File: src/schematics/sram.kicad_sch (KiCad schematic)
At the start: 4 parts, among them U9 IS61WV25616BLL-*BLI

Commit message: Add remaining component footprints (#79)
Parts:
- C90, C91, C92: footprint (none) -> Capacitor_SMD:C_0402_1005Metric
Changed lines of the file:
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@@
+		(polyline
+			(pts
+				(xy 165.1 74.93) (xy 165.1 115.57) (xy 167.64 115.57) (xy 167.64 74.93)
+			)
+			(stroke
+				(width 0)
+				(type dash)
+			)
+			(fill
+				(type color)
+				(color 255 0 0 0.1)
+			)
+		)
+	)
+	(rule_area
 		(polyline
 			(pts
 				(xy 135.89 64.77) (xy 135.89 124.46) (xy 138.43 124.46) (xy 138.43 64.77)
-			)
-			(stroke
-				(width 0)
-				(type dash)
-			)
-			(fill
-				(type color)
-				(color 255 0 0 0.1)
-			)
-		)
-	)
-	(rule_area
-		(polyline
-			(pts
-				(xy 165.1 74.93) (xy 165.1 115.57) (xy 167.64 115.57) (xy 167.64 74.93)
 			)
 			(stroke
@@
 			)
 		)
-		(property "Footprint" ""
+		(property "Footprint" "Capacitor_SMD:C_0402_1005Metric"
 			(at 166.37 53.34 0)
 			(effects
@@
 			)
 		)
-		(property "Footprint" ""
+		(property "Footprint" "Capacitor_SMD:C_0402_1005Metric"
 			(at 176.53 53.34 0)
 			(effects
@@
 			)
 		)
-		(property "Footprint" ""
+		(property "Footprint" "Capacitor_SMD:C_0402_1005Metric"
 			(at 186.69 53.34 0)
 			(effects

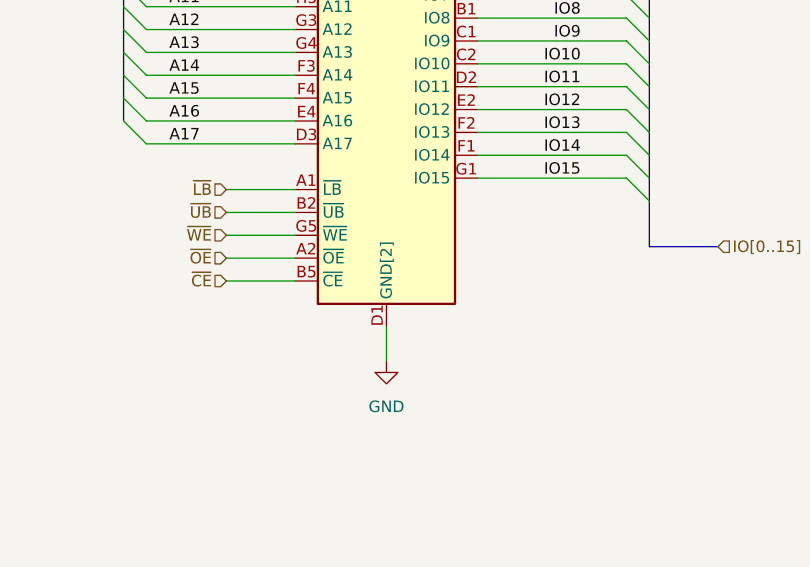
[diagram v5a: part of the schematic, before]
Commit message: Update big inductors for smaller ones
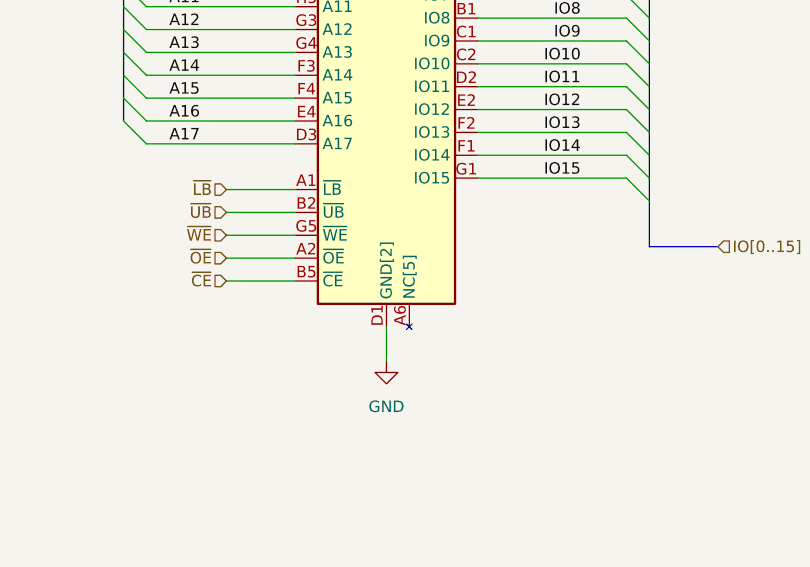
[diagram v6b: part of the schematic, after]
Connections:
- net at U9.A6 (NC[5]), U9.E3 (NC), U9.G2 (NC)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: no longer U9. (NC[5])
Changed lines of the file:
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@@
+		(polyline
+			(pts
+				(xy 135.89 64.77) (xy 135.89 124.46) (xy 138.43 124.46) (xy 138.43 64.77)
+			)
+			(stroke
+				(width 0)
+				(type dash)
+			)
+			(fill
+				(type color)
+				(color 255 0 0 0.1)
+			)
+		)
+	)
+	(rule_area
 		(polyline
 			(pts
 				(xy 165.1 74.93) (xy 165.1 115.57) (xy 167.64 115.57) (xy 167.64 74.93)
-			)
-			(stroke
-				(width 0)
-				(type dash)
-			)
-			(fill
-				(type color)
-				(color 255 0 0 0.1)
-			)
-		)
-	)
-	(rule_area
-		(polyline
-			(pts
-				(xy 135.89 64.77) (xy 135.89 124.46) (xy 138.43 124.46) (xy 138.43 64.77)
 			)
 			(stroke
@@
 		(pin "G5"
 		)
-		(pin ""
-		)
 		(pin "C1"
